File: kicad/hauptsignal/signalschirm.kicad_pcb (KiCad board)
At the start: 2 copper layers, 6.6 x 13.6 mm, 18 parts, among them J1 Conn_01x01_Male, J2 Conn_01x01_Male, J3 Conn_01x01_Male, J4 Conn_01x01_Male, J5 Conn_01x01_Male, J6 Conn_01x01_Male, J7 Conn_01x01_Male, J8 Conn_01x01_Male

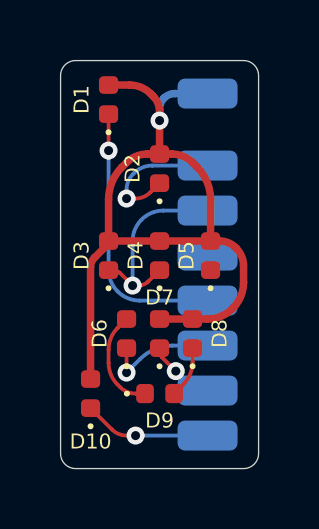
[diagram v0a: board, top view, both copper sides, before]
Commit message: Shrink PCB element size and add rounded tracks and teardrops
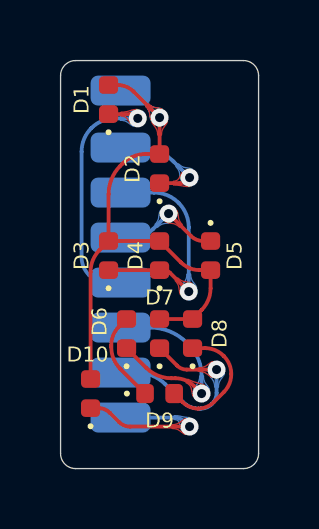
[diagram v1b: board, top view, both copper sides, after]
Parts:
- moved J2 2.96 mm to (122.0, 75.9)
- moved J3 2.96 mm to (122.0, 77.4)
- moved J4 2.96 mm to (122.0, 78.9)
- moved J5 2.96 mm to (122.0, 80.4)
- moved J6 2.96 mm to (122.0, 81.9)
- moved J7 2.96 mm to (122.0, 83.4)
- moved J8 2.96 mm to (122.0, 84.9)
- moved J1 2.90 mm to (122.0, 74.0)
- turned D5 to -90 degrees
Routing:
- net Net-(D2-Pad2): track 27.7 -> 20.7 mm
- net Net-(D7-Pad1): track 2.28 -> 6.84 mm
- net Net-(D6-Pad1): track 3.81 -> 7.19 mm
- net Net-(D5-Pad1): track 0.60 -> 3.64 mm, vias 0 -> 1
- net Net-(D9-Pad2): track 1.72 -> 4.46 mm
- net Net-(D10-Pad1): track 4.25 -> 5.90 mm
- net Net-(D3-Pad1): track 6.64 -> 8.02 mm
- net Net-(D2-Pad1): track 4.71 -> 3.70 mm
